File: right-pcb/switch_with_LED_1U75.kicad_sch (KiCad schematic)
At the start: 4 parts, among them SW19 SW_SPST

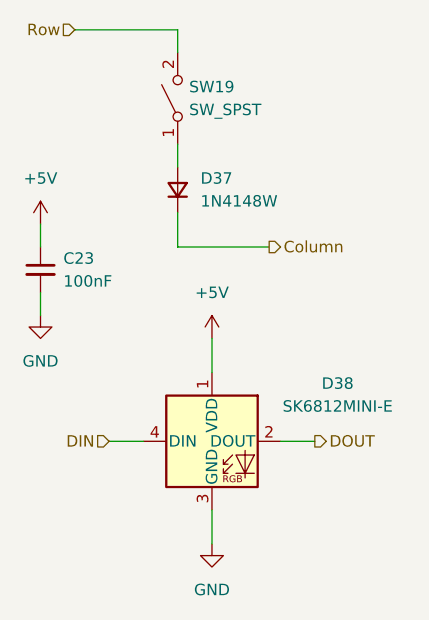
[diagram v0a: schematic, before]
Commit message: initial placement of switches and modifications from left to right
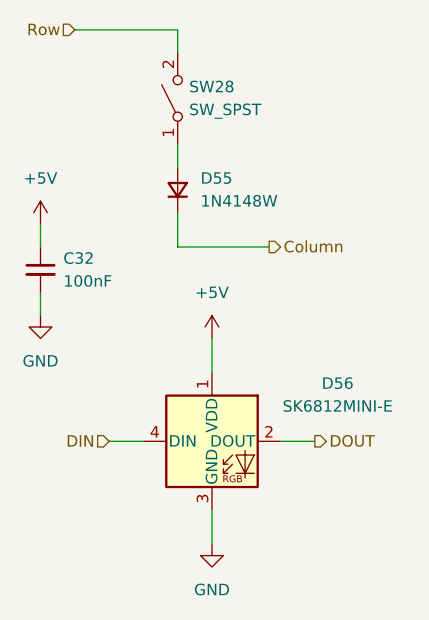
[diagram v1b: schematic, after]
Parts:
- renumbered C23 to C32, D37 to D55, D38 to D56, SW19 to SW28
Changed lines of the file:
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@@
 		(dnp no)
 		(fields_autoplaced yes)
-		(property "Reference" "D37"
+		(property "Reference" "D55"
 			(at 123.19 102.8699 90)
 			(effects
@@
 					(unit 1)
 				)
+				(path "/cf145565-22e2-4e5a-8a27-915862c57a1b/a95fd074-736b-466b-b448-0c214e98e022"
+					(reference "D55")
+					(unit 1)
+				)
 			)
 		)
@@
 		(dnp no)
 		(fields_autoplaced yes)
-		(property "Reference" "SW19"
+		(property "Reference" "SW28"
 			(at 121.92 92.7099 90)
 			(effects
@@
 					(unit 1)
 				)
+				(path "/cf145565-22e2-4e5a-8a27-915862c57a1b/a95fd074-736b-466b-b448-0c214e98e022"
+					(reference "SW28")
+					(unit 1)
+				)
 			)
 		)
@@
 		(dnp no)
 		(fields_autoplaced yes)
-		(property "Reference" "D38"
+		(property "Reference" "D56"
 			(at 138.43 125.6598 0)
 			(effects
@@
 					(unit 1)
 				)
+				(path "/cf145565-22e2-4e5a-8a27-915862c57a1b/a95fd074-736b-466b-b448-0c214e98e022"
+					(reference "D56")
+					(unit 1)
+				)
 			)
 		)
@@
 		(dnp no)
 		(fields_autoplaced yes)
-		(property "Reference" "#PWR092"
+		(property "Reference" "#PWR0128"
 			(at 124.46 149.86 0)
 			(effects
@@
 					(unit 1)
 				)
+				(path "/cf145565-22e2-4e5a-8a27-915862c57a1b/a95fd074-736b-466b-b448-0c214e98e022"
+					(reference "#PWR0128")
+					(unit 1)
+				)
 			)
 		)
@@
 		(dnp no)
 		(fields_autoplaced yes)
-		(property "Reference" "C23"
+		(property "Reference" "C32"
 			(at 107.95 111.7662 0)
 			(effects
@@
 					(unit 1)
 				)
+				(path "/cf145565-22e2-4e5a-8a27-915862c57a1b/a95fd074-736b-466b-b448-0c214e98e022"
+					(reference "C32")
+					(unit 1)
+				)
 			)
 		)
@@
 		(dnp no)
 		(fields_autoplaced yes)
-		(property "Reference" "#PWR089"
+		(property "Reference" "#PWR0125"
 			(at 105.41 111.76 0)
 			(effects
@@
 					(unit 1)
 				)
+				(path "/cf145565-22e2-4e5a-8a27-915862c57a1b/a95fd074-736b-466b-b448-0c214e98e022"
+					(reference "#PWR0125")
+					(unit 1)
+				)
 			)
 		)
@@
 		(dnp no)
 		(fields_autoplaced yes)
-		(property "Reference" "#PWR090"
+		(property "Reference" "#PWR0126"
 			(at 105.41 124.46 0)
 			(effects
@@
 					(unit 1)
 				)
+				(path "/cf145565-22e2-4e5a-8a27-915862c57a1b/a95fd074-736b-466b-b448-0c214e98e022"
+					(reference "#PWR0126")
+					(unit 1)
+				)
 			)
 		)
@@
 		(dnp no)
 		(fields_autoplaced yes)
-		(property "Reference" "#PWR091"
+		(property "Reference" "#PWR0127"
 			(at 124.46 124.46 0)
 			(effects
@@
 					(unit 1)
 				)
+				(path "/cf145565-22e2-4e5a-8a27-915862c57a1b/a95fd074-736b-466b-b448-0c214e98e022"
+					(reference "#PWR0127")
+					(unit 1)
+				)

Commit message: Boards were ordered
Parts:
- SW28: symbol Switch:SW_SPST -> SW-gElectroMech:SPST_MOM
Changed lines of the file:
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@@
 	)
 	(symbol
-		(lib_id "Switch:SW_SPST")
+		(lib_id "SW-gElectroMech:SPST_MOM")
 		(at 120.65 93.98 90)
 		(unit 1)
@@
 		)
 		(property "Datasheet" ""
-			(at 120.65 93.98 0)
+			(at 115.57 93.98 0)
 			(hide yes)
 			(show_name no)
@@
 			)
 		)
-		(property "Description" "Single Pole Single Throw (SPST) switch"
+		(property "Description" "Push button switch, generic, two pins"
 			(at 120.65 93.98 0)
 			(hide yes)
